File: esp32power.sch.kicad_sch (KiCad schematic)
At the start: 40 parts, among them Q1 MMBT3904, Q2 MMBT3904, U10 TL072, U11 TL072, U2 TPS72301DDC, U3 R-78E3.3-1.0, U5 NAU88C22YG, U6 TPS72301DDC, U7 TL072, U8 TL072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

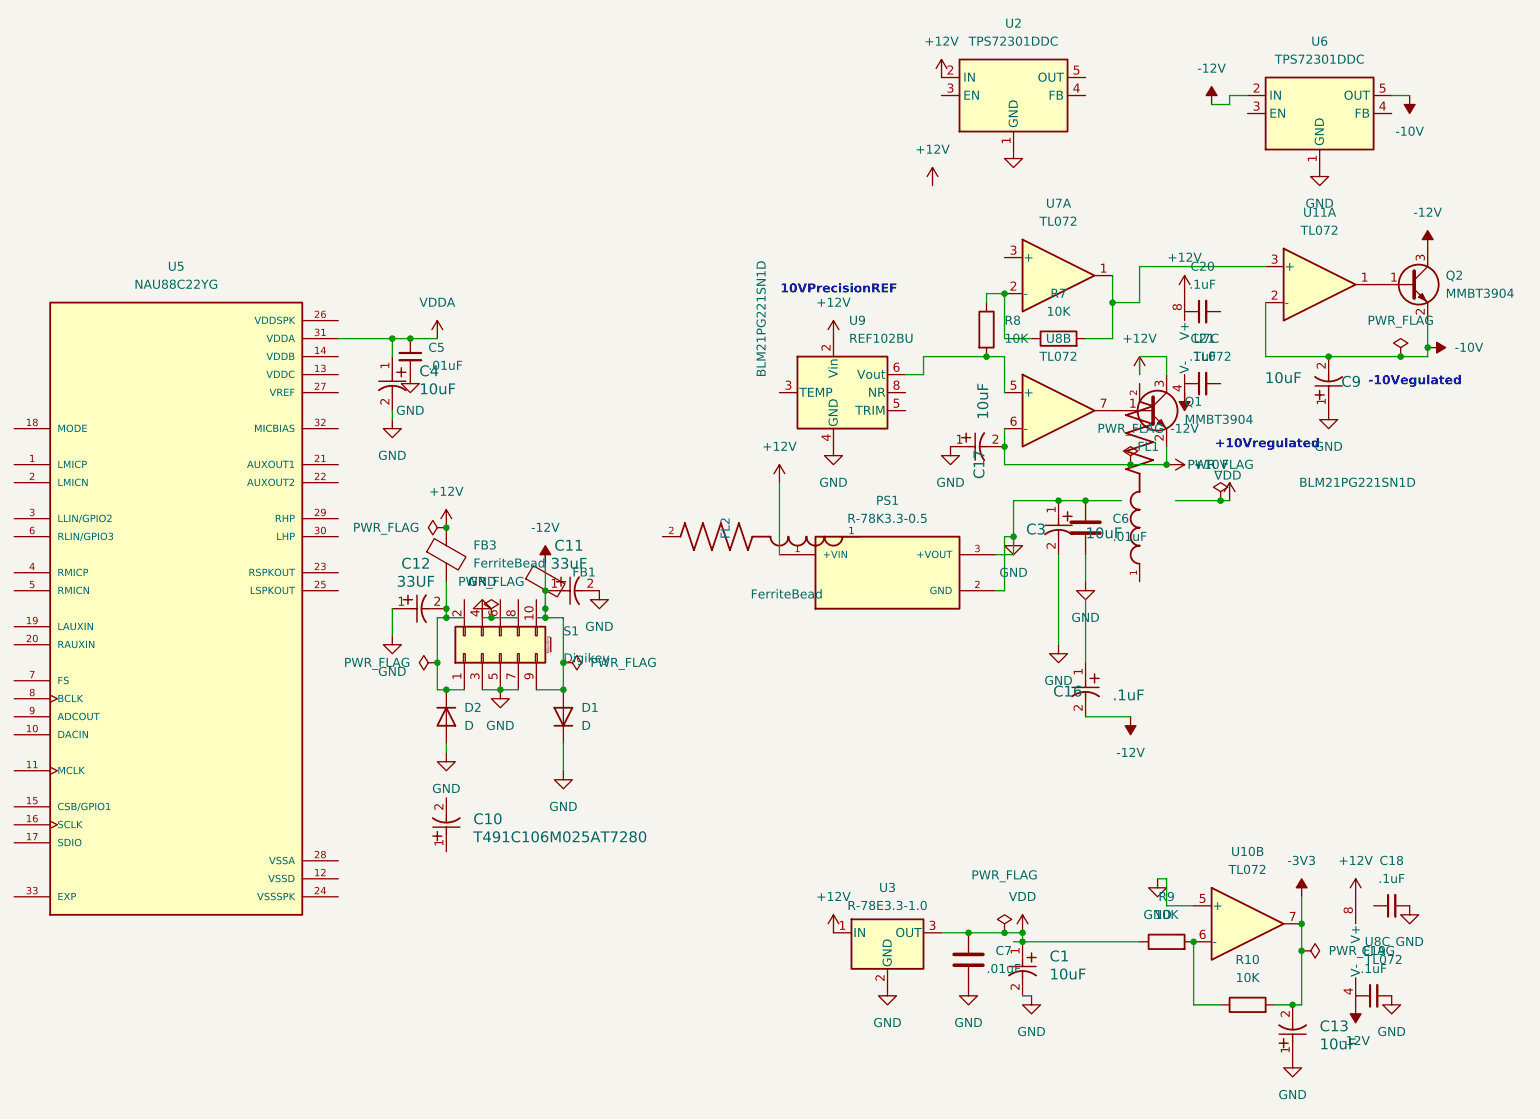
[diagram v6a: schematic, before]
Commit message: updated common lib symbols and footprint models
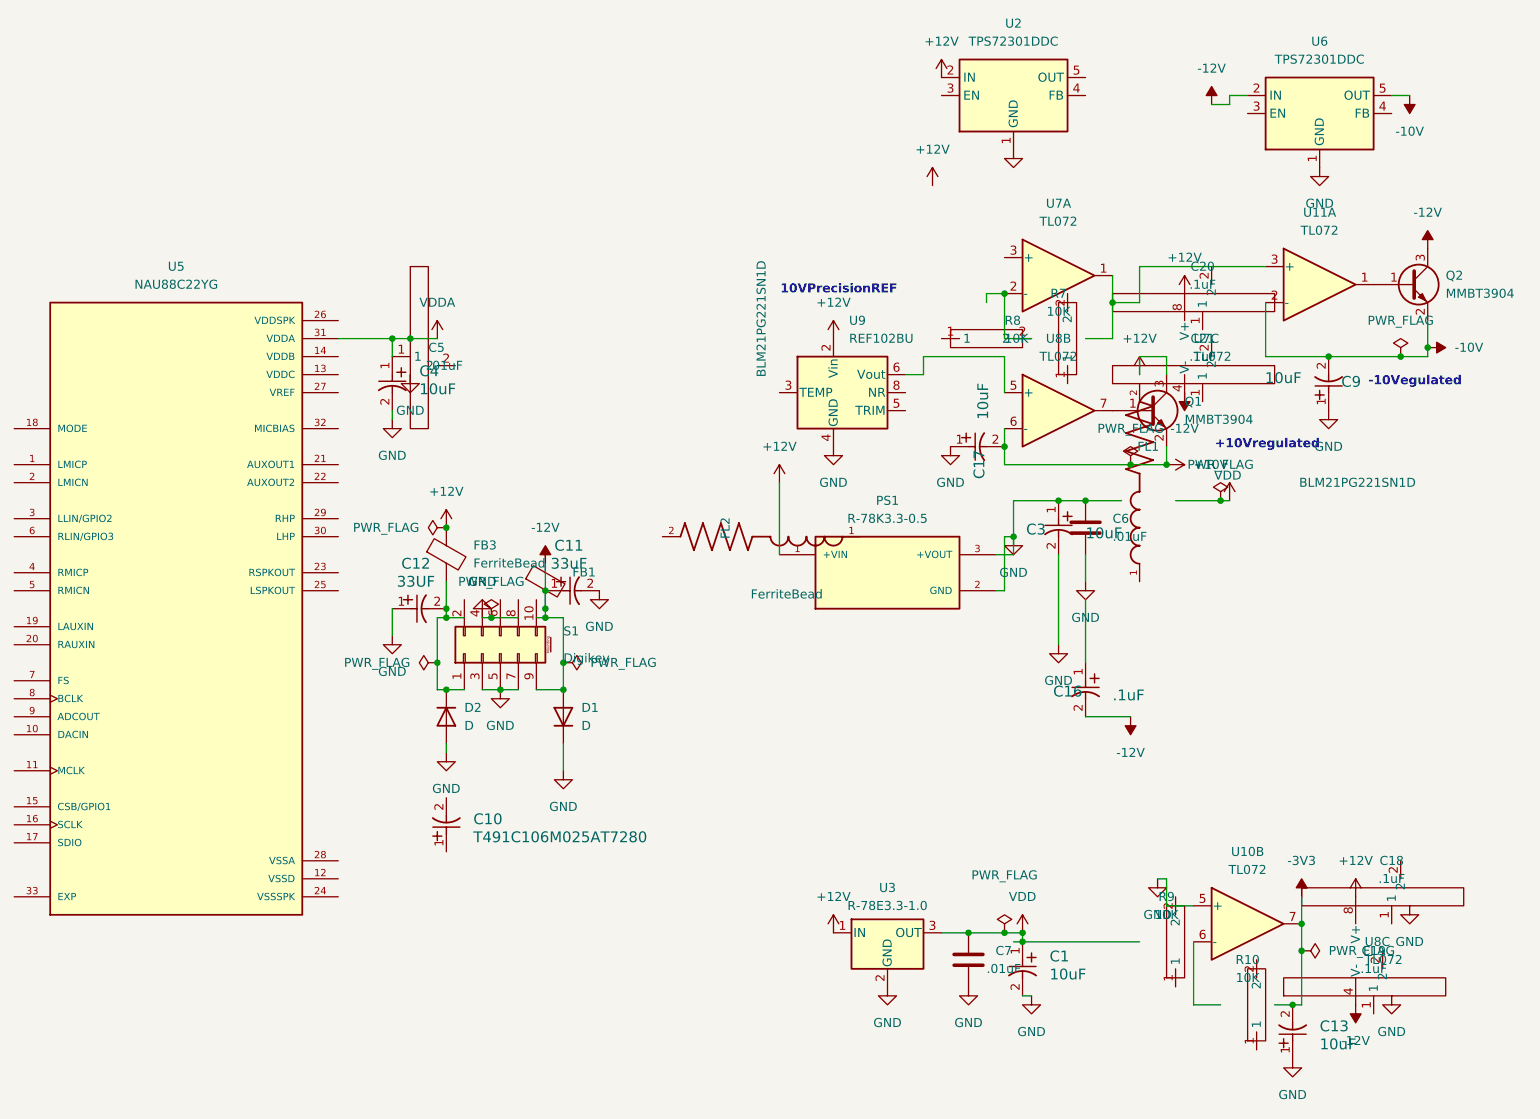
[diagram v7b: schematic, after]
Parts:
- C18, C19, C20, C21: footprint Capacitor_SMD:C_0603_1608Metric_Pad1.08x0.95mm_HandSolder -> commonfootprint:Ceramic0603; symbol Device:C_Small -> common:CerCap
- C5: footprint Capacitor_SMD:C_0603_1608Metric -> commonfootprint:Ceramic0603; symbol Device:C_Small -> common:CerCap
- R10, R7, R8, R9: footprint (none) -> commonfootprint:Modcan0603; symbol Device:R -> common:R
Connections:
- net -3V3: no longer R10.2
- net GND: no longer C18.2, C19.2, C5.2
- net VDD: no longer R9.1
- net at U11.3 (+), U7.1: no longer R7.2
- net at U8.5 (+), U9.6 (Vout): no longer R8.2
- new net: R8.2, U7.2 (-)
- now unconnected: R10.1, R7.1, R8.1, R9.2, U10.6 (-)
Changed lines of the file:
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@@
 	)
 	(junction
-		(at 242.57 147.32)
-		(diameter 0)
-		(color 0 0 0 0)
-	)
-	(junction
 		(at 151.13 101.6)
 		(diameter 0)
@@
 	)
 	(junction
-		(at 213.36 64.77)
-		(diameter 0)
-		(color 0 0 0 0)
-	)
-	(junction
 		(at 227.33 85.09)
 		(diameter 0)
@@
 	(wire
 		(pts
-			(xy 204.47 64.77) (xy 213.36 64.77)
+			(xy 204.47 64.77) (xy 215.9 64.77)
 		)
 		(stroke
@@
 	(wire
 		(pts
-			(xy 213.36 64.77) (xy 215.9 64.77)
-		)
-		(stroke
-			(width 0)
-			(type default)
-		)
-	)
-	(wire
-		(pts
 			(xy 135.89 101.6) (xy 137.16 101.6)
 		)
@@
 	)
 	(symbol
-		(lib_id "Device:R")
+		(lib_id "common:R")
 		(at 223.52 62.23 90)
 		(unit 1)
@@
 			)
 		)
-		(property "Footprint" ""
+		(property "Footprint" "commonfootprint:Modcan0603"
 			(at 223.52 64.008 90)
 			(effects
@@
 	)
 	(symbol
-		(lib_id "Device:C_Small")
+		(lib_id "common:CerCap")
 		(at 267.97 154.94 90)
 		(unit 1)
@@
 			)
 		)
-		(property "Footprint" "Capacitor_SMD:C_0603_1608Metric_Pad1.08x0.95mm_HandSolder"
+		(property "Footprint" "commonfootprint:Ceramic0603"
 			(at 267.97 154.94 0)
 			(effects
@@
 	)
 	(symbol
-		(lib_id "Device:R")
+		(lib_id "common:R")
 		(at 238.76 147.32 90)
 		(unit 1)
@@
 			)
 		)
-		(property "Footprint" ""
+		(property "Footprint" "commonfootprint:Modcan0603"
 			(at 238.76 149.098 90)
 			(effects
@@
 	)
 	(symbol
-		(lib_id "Device:C_Small")
+		(lib_id "common:CerCap")
 		(at 132.08 64.77 0)
 		(unit 1)
@@
 			)
 		)
-		(property "Footprint" "Capacitor_SMD:C_0603_1608Metric"
+		(property "Footprint" "commonfootprint:Ceramic0603"
 			(at 132.08 64.77 0)
 			(effects
@@
 	)
 	(symbol
-		(lib_id "Device:C_Small")
+		(lib_id "common:CerCap")
 		(at 270.51 142.24 90)
 		(unit 1)
@@
 			)
 		)
-		(property "Footprint" "Capacitor_SMD:C_0603_1608Metric_Pad1.08x0.95mm_HandSolder"
+		(property "Footprint" "commonfootprint:Ceramic0603"
 			(at 270.51 142.24 0)
 			(effects
@@
 	)
 	(symbol
-		(lib_id "Device:R")
+		(lib_id "common:R")
 		(at 250.19 156.21 90)
 		(unit 1)
@@
 			)
 		)
-		(property "Footprint" ""
+		(property "Footprint" "commonfootprint:Modcan0603"
 			(at 250.19 157.988 90)
 			(effects
@@
 	)
 	(symbol
-		(lib_id "Device:C_Small")
+		(lib_id "common:CerCap")
 		(at 243.84 58.42 90)
 		(unit 1)
@@
 			)
 		)
-		(property "Footprint" "Capacitor_SMD:C_0603_1608Metric_Pad1.08x0.95mm_HandSolder"
+		(property "Footprint" "commonfootprint:Ceramic0603"
 			(at 243.84 58.42 0)
 			(effects
@@
 	)
 	(symbol
-		(lib_id "Device:C_Small")
+		(lib_id "common:CerCap")
 		(at 243.84 68.58 90)
 		(unit 1)
@@
 			)
 		)
-		(property "Footprint" "Capacitor_SMD:C_0603_1608Metric_Pad1.08x0.95mm_HandSolder"
+		(property "Footprint" "commonfootprint:Ceramic0603"
 			(at 243.84 68.58 0)
 			(effects
@@
 	)
 	(symbol
-		(lib_id "Device:R")
+		(lib_id "common:R")
 		(at 213.36 60.96 0)
 		(unit 1)
@@
 			)
 		)
-		(property "Footprint" ""
+		(property "Footprint" "commonfootprint:Modcan0603"
 			(at 211.582 60.96 90)
 			(effects

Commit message: updated a few caps
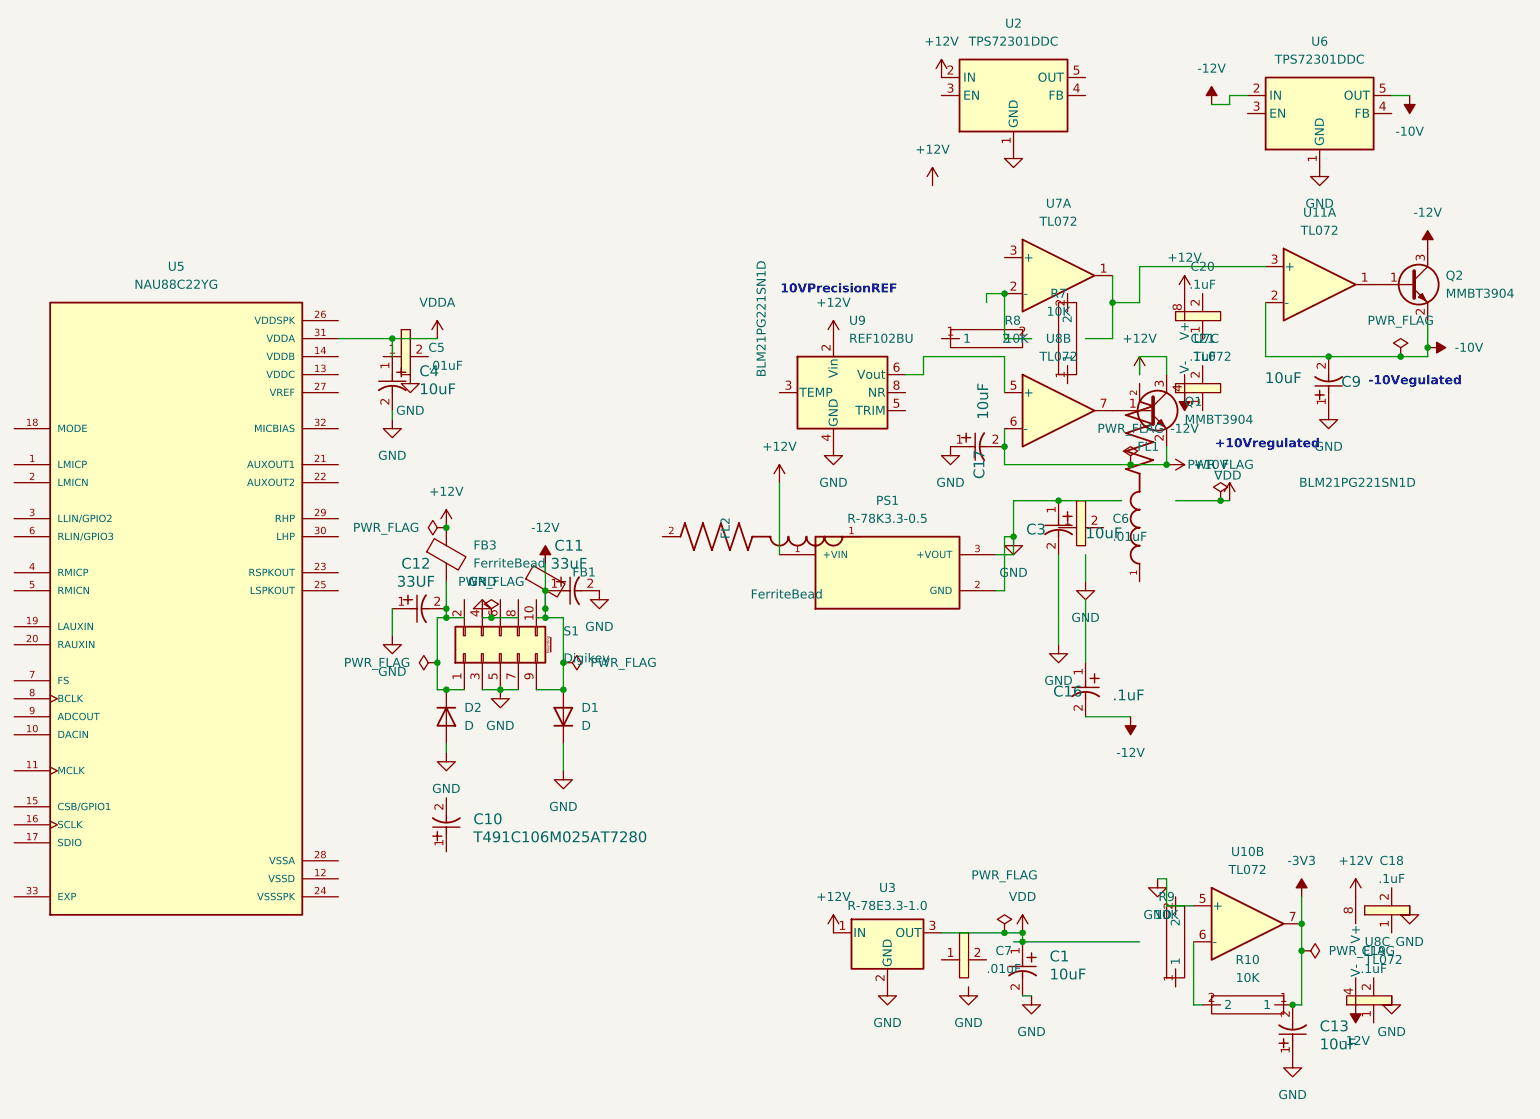
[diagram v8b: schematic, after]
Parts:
- C6, C7: footprint (none) -> commonfootprint:Ceramic0603; symbol Device:C -> common:CerCap
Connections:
- net -3V3: now also R10.1
- net GND: no longer C6.1, C6.2, C7.2
- net VDD: no longer C7.1
- net VDDA: no longer C5.1
- net at R10.2: now also U10.6 (-)
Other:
- moved on the sheet: R10
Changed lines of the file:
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@@
 	)
 	(junction
-		(at 227.33 85.09)
-		(diameter 0)
-		(color 0 0 0 0)
-	)
-	(junction
-		(at 210.82 146.05)
-		(diameter 0)
-		(color 0 0 0 0)
-	)
-	(junction
 		(at 223.52 85.09)
 		(diameter 0)
@@
 	)
 	(junction
-		(at 132.08 62.23)
-		(diameter 0)
-		(color 0 0 0 0)
-	)
-	(junction
 		(at 233.68 80.01)
 		(diameter 0)
@@
 	(wire
 		(pts
-			(xy 210.82 146.05) (xy 207.01 146.05)
+			(xy 207.01 146.05) (xy 215.9 146.05)
 		)
 		(stroke
@@
 	(wire
 		(pts
-			(xy 215.9 146.05) (xy 210.82 146.05)
+			(xy 151.13 100.33) (xy 151.13 101.6)
 		)
 		(stroke
@@
 	(wire
 		(pts
-			(xy 151.13 100.33) (xy 151.13 101.6)
+			(xy 129.54 64.77) (xy 129.54 62.23)
 		)
 		(stroke
@@
 	(wire
 		(pts
-			(xy 129.54 64.77) (xy 129.54 62.23)
+			(xy 135.89 111.76) (xy 135.89 107.95)
 		)
 		(stroke
@@
 	(wire
 		(pts
-			(xy 135.89 111.76) (xy 135.89 107.95)
+			(xy 237.49 138.43) (xy 238.76 138.43)
 		)
 		(stroke
@@
 	(wire
 		(pts
-			(xy 237.49 138.43) (xy 238.76 138.43)
+			(xy 257.81 144.78) (xy 257.81 148.59)
 		)
 		(stroke
@@
 	(wire
 		(pts
-			(xy 257.81 144.78) (xy 257.81 148.59)
+			(xy 245.11 29.21) (xy 247.65 29.21)
 		)
 		(stroke
@@
 	(wire
 		(pts
-			(xy 245.11 29.21) (xy 247.65 29.21)
+			(xy 243.84 156.21) (xy 242.57 156.21)
 		)
 		(stroke
@@
 	(wire
 		(pts
-			(xy 254 156.21) (xy 256.54 156.21)
-		)
-		(stroke
-			(width 0)
-			(type default)
-		)
-	)
-	(wire
-		(pts
 			(xy 137.16 120.65) (xy 137.16 119.38)
 		)
@@
 	(wire
 		(pts
-			(xy 246.38 156.21) (xy 242.57 156.21)
-		)
-		(stroke
-			(width 0)
-			(type default)
-		)
-	)
-	(wire
-		(pts
 			(xy 217.17 85.09) (xy 223.52 85.09)
 		)
@@
 	(wire
 		(pts
-			(xy 227.33 85.09) (xy 232.41 85.09)
-		)
-		(stroke
-			(width 0)
-			(type default)
-		)
-	)
-	(wire
-		(pts
 			(xy 234.95 52.07) (xy 234.95 57.15)
 		)
@@
 	(wire
 		(pts
-			(xy 223.52 85.09) (xy 227.33 85.09)
+			(xy 223.52 85.09) (xy 232.41 85.09)
 		)
 		(stroke
@@
 	(wire
 		(pts
-			(xy 132.08 62.23) (xy 135.89 62.23)
-		)
-		(stroke
-			(width 0)
-			(type default)
-		)
-	)
-	(wire
-		(pts
 			(xy 151.13 97.79) (xy 151.13 100.33)
 		)
@@
 	(wire
 		(pts
-			(xy 129.54 62.23) (xy 132.08 62.23)
+			(xy 129.54 62.23) (xy 135.89 62.23)
 		)
 		(stroke
@@
 	)
 	(symbol
-		(lib_id "Device:C")
+		(lib_id "common:CerCap")
 		(at 210.82 149.86 0)
 		(unit 1)
@@
 			)
 		)
-		(property "Footprint" ""
+		(property "Footprint" "commonfootprint:Ceramic0603"
 			(at 211.7852 153.67 0)
 			(effects
@@
 	)
 	(symbol
-		(lib_id "Device:C")
+		(lib_id "common:CerCap")
 		(at 227.33 88.9 0)
 		(unit 1)
@@
 			)
 		)
-		(property "Footprint" ""
+		(property "Footprint" "commonfootprint:Ceramic0603"
 			(at 228.2952 92.71 0)
 			(effects
@@
 	(symbol
 		(lib_id "common:R")
-		(at 250.19 156.21 90)
+		(at 250.19 157.48 180)
 		(unit 1)
 		(exclude_from_sim no)
@@
 		(fields_autoplaced yes)
 		(property "Reference" "R10"
-			(at 250.19 149.86 90)
+			(at 250.19 149.86 0)
 			(effects
 				(font
@@
 		)
 		(property "Value" "10K"
-			(at 250.19 152.4 90)
+			(at 250.19 152.4 0)
 			(effects
 				(font
@@
 		)
 		(property "Footprint" "commonfootprint:Modcan0603"
-			(at 250.19 157.988 90)
+			(at 251.968 157.48 90)
 			(effects
 				(font
@@
 		)
 		(property "Datasheet" "~"
-			(at 250.19 156.21 0)
+			(at 250.19 157.48 0)
 			(effects
 				(font
@@
 		)
 		(property "Description" "Resistor"
-			(at 250.19 156.21 0)
+			(at 250.19 157.48 0)
 			(effects
 				(font
